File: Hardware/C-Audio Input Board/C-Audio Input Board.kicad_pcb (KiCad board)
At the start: 2 copper layers, 197 x 40 mm, 50 parts, among them J1 XLR-In1 L, J10 GND, J11 XLR1_R, J12 XLR-In1 L, J13 XLR-In1 R, J14 +, J15 -, J16 GND, J17 XLR1_L, J18 XLR1, J19 +, J2 XLR-In1 R, J20 -, J21 GND, J22 XLR1_R, J23 Chinch-In1, J24 +, J25 -, J26 GND, J27 Chinch1, J28 Chinch-In1, J29 +, J3 +, J30 -, J31 GND, J32 Chinch1, J33 3.5mm, J34 +, J35 -, J36 GND, J37 +_sw, J38 -_sw, J39 Conn_01x05_Socket, J4 -, J40 Conn_01x03_Socket, J5 GND, J6 XLR1_L, J7 XLR1, J8 +, J9 -

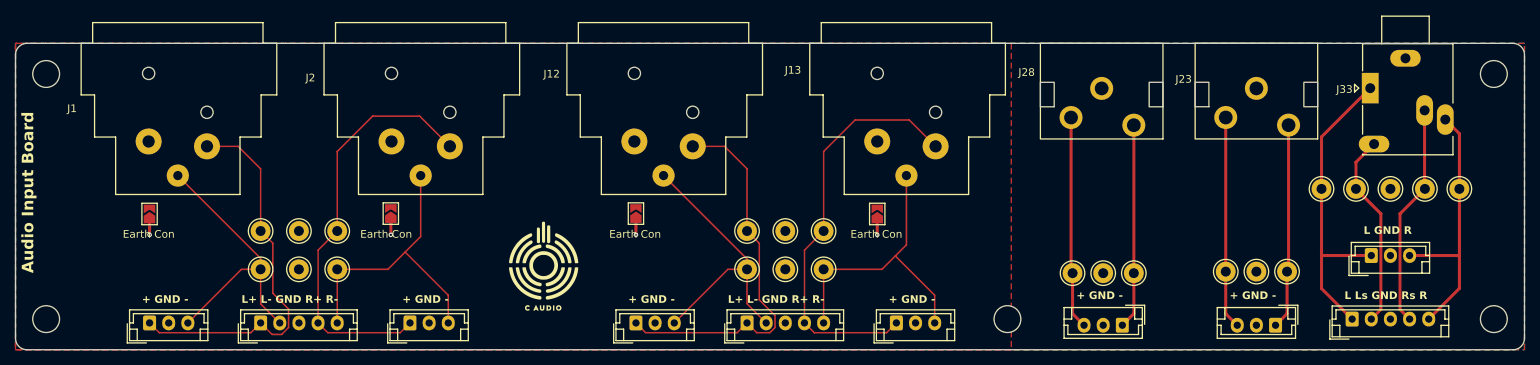
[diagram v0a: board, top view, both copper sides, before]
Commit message: added pentaconn and silkscreen marking. Also added PCBWay logo for sponsorship
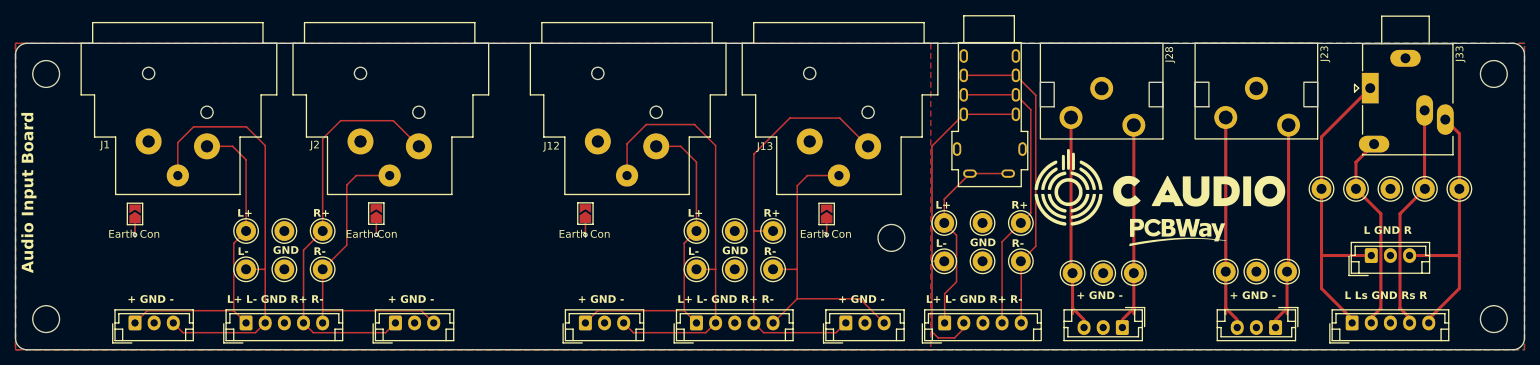
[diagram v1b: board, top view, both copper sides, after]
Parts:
- removed the G*** at (118.5, 84.0)
- added G***: LOGO, Footprints:C-Audio-LOGO, F.Cu at (198.9, 73.8)
- added G***: LOGO, Logos:pcbWay_logo_15mm, F.Cu at (201.1, 79.6)
- added J49: Pentaconn, Connectors Audio Chinch:Pentaconn, F.Cu at (176.6, 63.2)
- added J52: +, Connector_Pin:Pin_D1.3mm_L11.0mm, F.Cu at (170.8, 78.5)
- added J53: -, Connector_Pin:Pin_D1.3mm_L11.0mm, F.Cu at (170.8, 83.5)
- added J54: GND, Connector_Pin:Pin_D1.3mm_L11.0mm, F.Cu at (175.8, 83.5)
- added J56: PC, Connector_JST:JST_EH_B5B-EH-A_1x05_P2.50mm_Vertical, F.Cu at (170.8, 91.5)
- added J57: +, Connector_Pin:Pin_D1.3mm_L11.0mm, F.Cu at (180.8, 78.5)
- added J58: -, Connector_Pin:Pin_D1.3mm_L11.0mm, F.Cu at (180.8, 83.5)
- added J59: GND, Connector_Pin:Pin_D1.3mm_L11.0mm, F.Cu at (175.8, 78.5)
- J33: value 3.5mm -> 3.5mm
- moved H5 18.5 mm to (163.8, 80.4)
- moved J13 8.81 mm to (153.2, 67.8)
- moved J14 6.60 mm to (138.4, 79.5)
- moved J15 6.60 mm to (138.4, 84.5)
- moved J16 6.60 mm to (143.4, 84.5)
- moved J17 6.60 mm to (123.9, 91.5)
- moved J18 6.60 mm to (138.4, 91.5)
- moved J19 6.60 mm to (148.4, 79.5)
- moved J20 6.60 mm to (148.4, 84.5)
- moved J21 6.60 mm to (143.4, 79.5)
- moved J22 6.60 mm to (157.9, 91.5)
- moved JP3 6.60 mm to (123.9, 77.2)
- moved JP4 6.60 mm to (155.4, 77.3)
- moved J12 4.77 mm to (125.5, 67.8)
- moved J2 4.05 mm to (94.5, 67.8)
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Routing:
- net /Pentaconn/In-_L_PC: track 0.00 -> 44.2 mm
- net /Pentaconn/In-_R_PC: track 0.00 -> 41.0 mm
- net /Pentaconn/In+_R_PC: track 0.00 -> 38.9 mm
- net /Pentaconn/In+_L_PC: track 0.00 -> 27.2 mm
- net /XLR2/In-_L_XLR1: track 37.2 -> 56.6 mm
- net /XLR1/In-_L_XLR1: track 37.2 -> 56.3 mm
- net /XLR1/In+_L_XLR1: track 50.6 -> 42.0 mm
- net /XLR2/In+_L_XLR1: track 50.5 -> 42.0 mm
- net /XLR2/In-_R_XLR1: track 39.1 -> 41.0 mm
- net /XLR2/In+_R_XLR1: track 54.2 -> 56.0 mm
- net /XLR1/In+_R_XLR1: track 54.7 -> 53.1 mm
- net /XLR1/In-_R_XLR1: track 39.2 -> 40.6 mm
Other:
- board text added: "GND"
- board text added: "L+"
- board text added: "L-"
- board text added: "R+"
- board text added: "R-"

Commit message: added BOM and new gerbers
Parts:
- moved G*** 1.36 mm to (200.2, 74.0)
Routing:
- net /3.5mm/In_L_3.5_sw: track 25.7 -> 26.2 mm
- net /3.5mm/In_R_3.5_sw: track 29.1 -> 29.6 mm
- net /3.5mm/In_R_3.5: track 35.0 -> 35.5 mm
- net /3.5mm/In_L_3.5: track 40.9 -> 41.4 mm
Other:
- board text added: "L Lsw GND Rsw R"
- board text removed: "L Ls GND Rs R"
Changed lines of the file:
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@@
 			(drillshape 0)
 			(scaleselection 1)
-			(outputdirectory "Gerbers/")
+			(outputdirectory "../../Production/")
 		)
 	)
@@
 	(footprint "Footprints:C-Audio-LOGO"
 		(layer "F.Cu")
-		(at 198.9 73.8)
+		(at 200.25 74)
 		(property "Reference" "G***"
 			(at 0 0 0)
@@
 		(at 176.6 63.2 180)
 		(property "Reference" "J49"
-			(at 33.3 -37.35 180)
+			(at -5.15 6.95 90)
 			(unlocked yes)
 			(layer "F.SilkS")
-			(hide yes)
 			(effects
 				(font
@@
 	)
 	(gr_text "+ GND -"
-		(at 188 88.5 0)
+		(at 188 89 0)
 		(layer "F.SilkS" knockout)
 		(effects
@@
 		)
 	)
-	(gr_text "L Ls GND Rs R"
-		(at 223 88.5 0)
+	(gr_text "L Lsw GND Rsw R"
+		(at 222.25 89 0)
 		(layer "F.SilkS" knockout)
 		(effects
@@
 		)
 	)
+	(gr_text "L Lsw GND Rsw R"
+		(at 219.57806 72.071517 0)
+		(layer "F.SilkS" knockout)
+		(effects
+			(font
+				(size 1.4 1.4)
+				(thickness 0.3)
+				(bold yes)
+			)
+			(justify left bottom)
+		)
+	)
 	(gr_text "L+\n"
 		(at 169.6 76.7 0)
@@
 	)
 	(gr_text "+ GND -"
-		(at 208 88.5 0)
+		(at 208 89 0)
 		(layer "F.SilkS" knockout)
 		(effects
@@
 	)
 	(segment
-		(start 215.5 89.575)
-		(end 214 91.075)
+		(start 215.5 84.8)
+		(end 215.5 89.575)
 		(width 0.4)
 		(layer "F.Cu")
@@
 	)
 	(segment
-		(start 215.5 84.8)
-		(end 215.5 90.3)
+		(start 214 91.075)
+		(end 214 92.1)
 		(width 0.4)
 		(layer "F.Cu")
@@
 	)
 	(segment
+		(start 215.5 89.575)
+		(end 214 91.075)
+		(width 0.4)
+		(layer "F.Cu")
+		(net 11)
+	)
+	(segment
 		(start 207.5 89.575)
 		(end 209 91.075)
@@
 	(segment
 		(start 207.5 84.8)
-		(end 207.5 90.3)
+		(end 207.5 89.575)
+		(width 0.4)
+		(layer "F.Cu")
+		(net 12)
+	)
+	(segment
+		(start 209 91.075)
+		(end 209 92.1)
 		(width 0.4)
 		(layer "F.Cu")
@@
 	)
 	(segment
+		(start 189 91.075)
+		(end 189 92.1)
+		(width 0.4)
+		(layer "F.Cu")
+		(net 13)
+	)
+	(segment
 		(start 187.3 64.683007)
 		(end 187.3 84.8)
@@
 	)
 	(segment
-		(start 187.5 85)
-		(end 187.5 90.3)
+		(start 187.3 84.8)
+		(end 187.5 85)
 		(width 0.4)
 		(layer "F.Cu")
@@
 	)
 	(segment
-		(start 187.3 84.8)
-		(end 187.5 85)
+		(start 187.5 85)
+		(end 187.5 89.575)
 		(width 0.4)
 		(layer "F.Cu")
@@
 	)
 	(segment
+		(start 195.5 65.683007)
+		(end 195.5 85)
+		(width 0.4)
+		(layer "F.Cu")
+		(net 14)
+	)
+	(segment
 		(start 195.5 89.575)
 		(end 194 91.075)
@@
 	)
 	(segment
-		(start 195.5 65.683007)
-		(end 195.5 85)
+		(start 195.5 85)
+		(end 195.5 89.575)
 		(width 0.4)
 		(layer "F.Cu")
@@
 	)
 	(segment
-		(start 195.5 85)
-		(end 195.5 90.3)
+		(start 194 91.075)
+		(end 194 92.1)
 		(width 0.4)
 		(layer "F.Cu")
@@
 	)
 	(segment
-		(start 233.5 74)
-		(end 230.25 77.25)
+		(start 231.5 90.825)
+		(end 231.5 91.5)
 		(width 0.4)
 		(layer "F.Cu")
@@
 	)
 	(segment
+		(start 233.5 74)
+		(end 230.25 77.25)
+		(width 0.4)
+		(layer "F.Cu")
+		(net 15)
+	)
+	(segment
+		(start 230.25 89.575)
+		(end 231.5 90.825)
+		(width 0.4)
+		(layer "F.Cu")
+		(net 15)
+	)
+	(segment
 		(start 230.25 77.25)
-		(end 230.25 89.75)
+		(end 230.25 89.575)
 		(width 0.4)
 		(layer "F.Cu")
@@
 	)
 	(segment
-		(start 230.25 89.575)
-		(end 231.5 90.825)
+		(start 227.75 89.575)
+		(end 226.5 90.825)
 		(width 0.4)
 		(layer "F.Cu")
-		(net 15)
+		(net 16)
 	)
 	(segment
@@
 	)
 	(segment
-		(start 224.5 70.512487)
-		(end 224.5 74)
+		(start 227.75 77.25)
+		(end 227.75 89.575)
 		(width 0.4)
 		(layer "F.Cu")
@@
 	)
 	(segment
-		(start 224.5 74)
-		(end 227.75 77.25)
+		(start 226.5 90.825)
+		(end 226.5 91.5)
 		(width 0.4)
 		(layer "F.Cu")
@@
 	)
 	(segment
-		(start 227.75 89.575)
-		(end 226.5 90.825)
+		(start 224.5 74)
+		(end 227.75 77.25)
 		(width 0.4)
 		(layer "F.Cu")
@@
 	)
 	(segment
-		(start 227.75 77.25)
-		(end 227.75 89.75)
+		(start 224.5 70.512487)
+		(end 224.5 74)
 		(width 0.4)
 		(layer "F.Cu")
@@
 	)
 	(segment
+		(start 234 91)
+		(end 234 91.5)
+		(width 0.4)
+		(layer "F.Cu")
+		(net 17)
+	)
+	(segment
 		(start 238 74)
 		(end 238 82.7)
@@
 	)
 	(segment
-		(start 220 87)
-		(end 224 91)
+		(start 224 91)
+		(end 224 91.5)
 		(width 0.4)
 		(layer "F.Cu")
@@
 	)
 	(segment
-		(start 220 82.7)
-		(end 220 87)
+		(start 220 87)
+		(end 224 91)
 		(width 0.4)
 		(layer "F.Cu")
@@
 		(width 0.4)
 		(layer "F.Cu")
+		(net 18)
+	)
+	(segment
+		(start 220 82.7)
+		(end 220 87)
+		(width 0.4)
+		(layer "F.Cu")

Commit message: finalized Silkscreen and production data
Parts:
- removed JP2, JP3, JP4: Earth Conn, Jumper:SolderJumper-2_P1.3mm_Open_TrianglePad1.0x1.5mm
- added REF**: OSHW-Logo2_7.3x6mm_SilkScreen, Symbol:OSHW-Logo2_7.3x6mm_SilkScreen, B.Cu at (120.7, 81.6)
- added REF**: KiCad-Logo2_5mm_SilkScreen, Symbol:KiCad-Logo2_5mm_SilkScreen, B.Cu at (108.8, 81.7)
- moved JP1 102.2 mm to (166.9, 85.9), turned to 180 degrees
- moved G*** 87.2 mm to (114.1, 85.8)
- moved G*** 87.2 mm to (113.2, 80.2)
- moved J23 0.17 mm to (211.2, 54.5)
- moved J28 0.17 mm to (191.0, 54.5)
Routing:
- net GND: track 8.10 -> 0.00 mm
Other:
- board text removed: "Audio Input Board"
